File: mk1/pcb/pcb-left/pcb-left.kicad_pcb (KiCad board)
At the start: 2 copper layers, 124.8 x 104.5 mm, 45 parts, among them J1 BAT, J2 Conn_01x05_Socket, SW1 SW_SPDT, U1 MCU

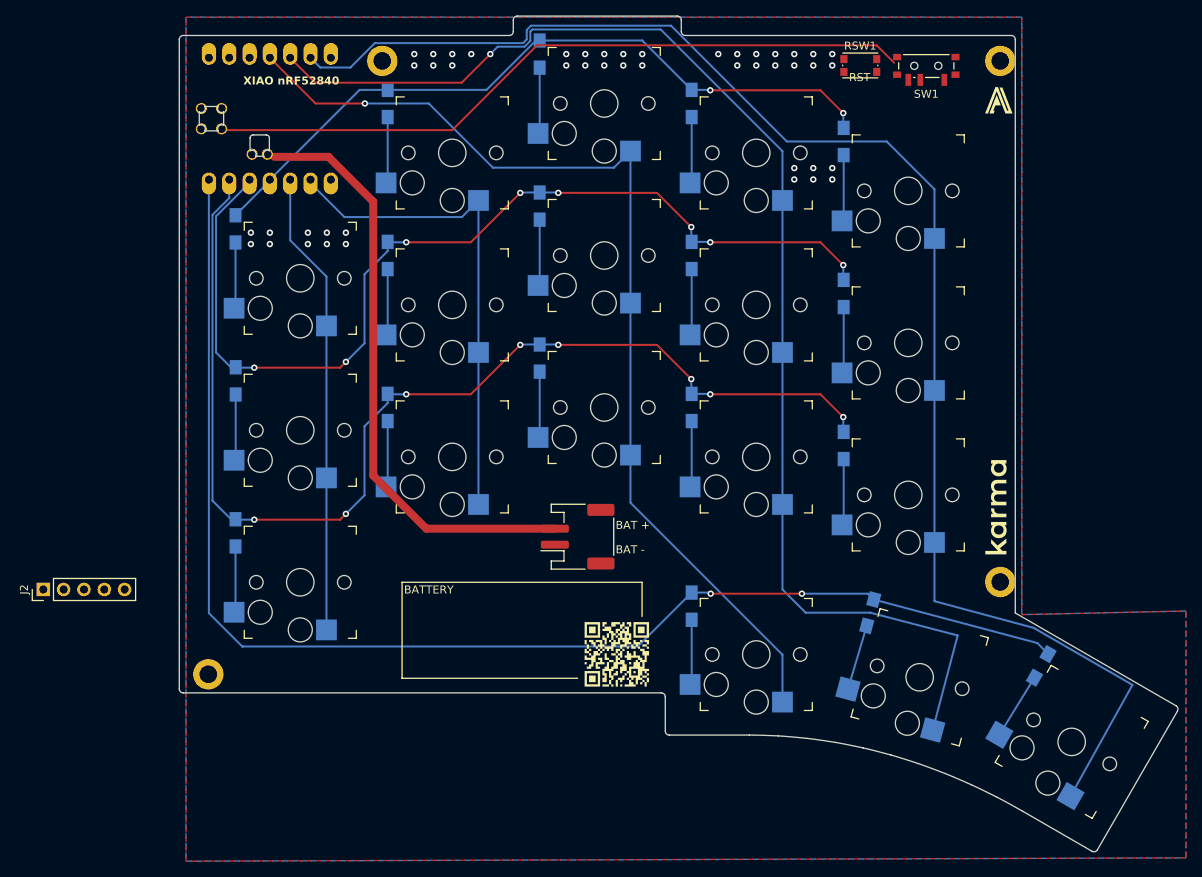
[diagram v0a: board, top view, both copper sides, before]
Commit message: mk1/pcb: revert pcb-left to earlier version
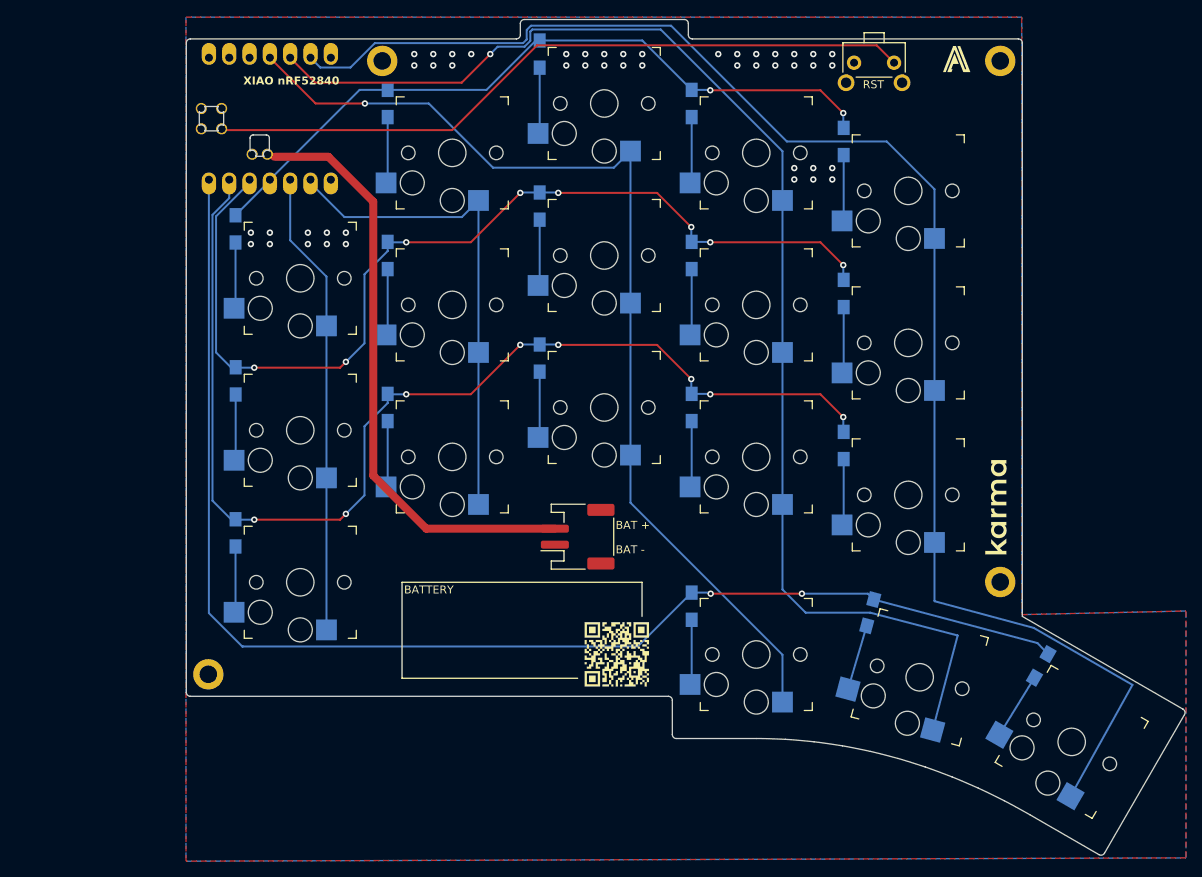
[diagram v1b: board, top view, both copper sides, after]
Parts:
- removed J2: Conn_01x05_Socket, Connector_PinHeader_2.54mm:PinHeader_1x05_P2.54mm_Vertical
- removed SW1: SW_SPDT, Button_Switch_SMD:SW_SPDT_PCM12
- RSW1: footprint Button_Switch_SMD:SW_Push_1P1T_NO_CK_KMR2 -> karmalib:SKHLLCA010
- U1: value MCU -> xiao-ble
- moved RSW1 1.95 mm to (123.7, 40.1)
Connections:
- U1 pad 12: 3V3_L -> unconnected-(U1-3V3-Pad12)
- U1 pad 15: SWDIO_L -> unconnected-(U1-A31_SWDIO-Pad15)
- U1 pad 16: SWDCLK_L -> unconnected-(U1-A30_SWCLK-Pad16)
- U1 pad 19: VSW_L -> VBAT_L
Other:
- outline, holes or cut-outs redrawn

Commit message: mk1/pcb-left: add power switch and debug header, update reset button
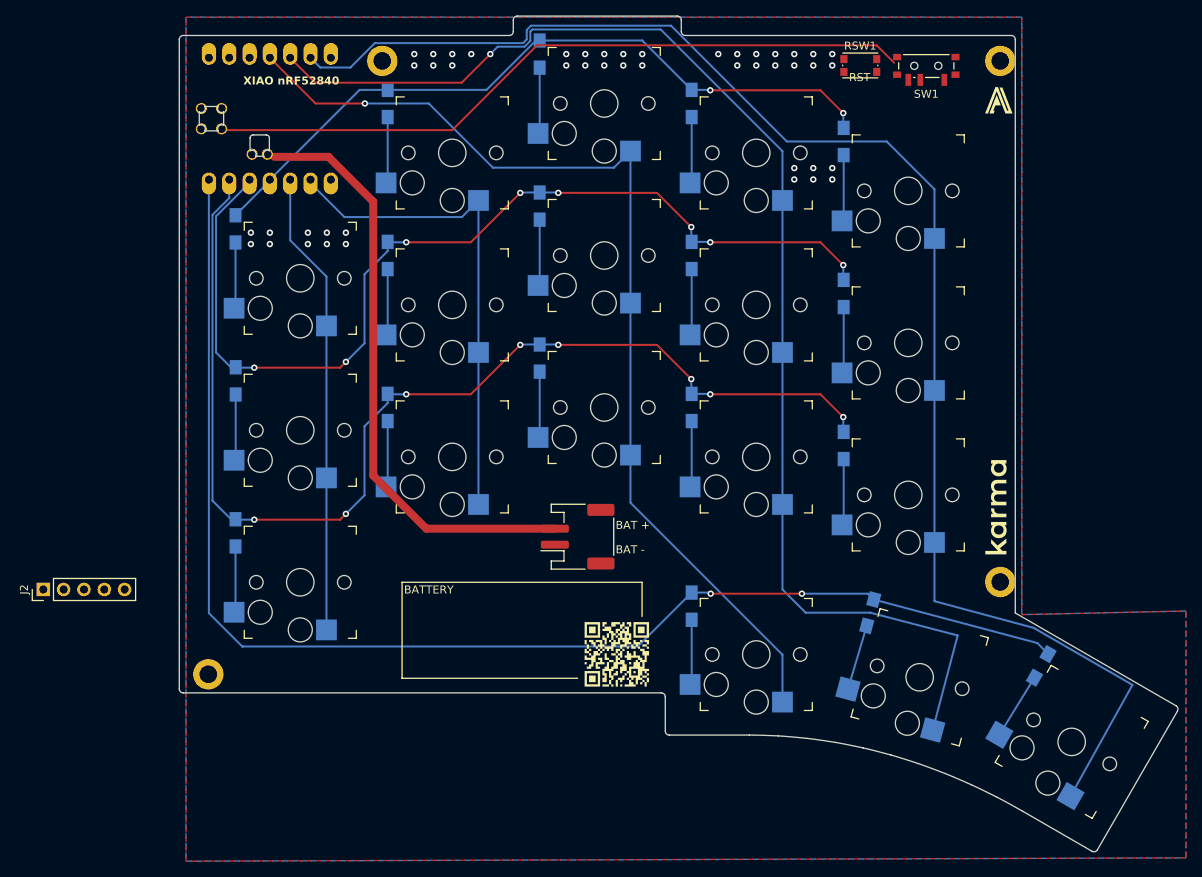
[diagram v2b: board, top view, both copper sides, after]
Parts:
- added J2: Conn_01x05_Socket, Connector_PinHeader_2.54mm:PinHeader_1x05_P2.54mm_Vertical, F.Cu at (19.9, 104.7)
- added SW1: SW_SPDT, Button_Switch_SMD:SW_SPDT_PCM12, F.Cu at (130.3, 39.5)
- RSW1: footprint karmalib:SKHLLCA010 -> Button_Switch_SMD:SW_Push_1P1T_NO_CK_KMR2
- U1: value xiao-ble -> MCU
- moved RSW1 1.95 mm to (122.0, 39.2)
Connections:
- U1 pad 12: unconnected-(U1-3V3-Pad12) -> 3V3_L
- U1 pad 15: unconnected-(U1-A31_SWDIO-Pad15) -> SWDIO_L
- U1 pad 16: unconnected-(U1-A30_SWCLK-Pad16) -> SWDCLK_L
- U1 pad 19: VBAT_L -> VSW_L
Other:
- outline, holes or cut-outs redrawn
